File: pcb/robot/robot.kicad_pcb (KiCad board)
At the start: 4 copper layers, 80 x 70 mm, 314 parts, among them IC1 TPS22998RYZR, J1 USBC_Receptacle_SMD_RA, J2 Conn_01x05, J3 Conn_01x06_MountingPin, J4 USB4151-GF-C, J5 Conn_01x06_MountingPin, J8 Conn_01x02, J9 Conn_01x16, Q1 Q_NMOS_GDS, Q2 EFC8811R-TF, Q3 AS2312, Q4 YJL3416A, Q5 SN74AHC125RGYR, Q6 SN74AHC125RGYR, Q7 Q_NMOS_GDS, SW1 SW_SPST, U1 STWLC38JRM, U10 TPS63021DSJR, U11 XC6206PxxxMR, U12 BQ27742YZFR-G1, U13 MAX77976EFD+, U18 AP33771DKZ-13, U2 W25Q128JVS, U25 TVS0500DRV, U26 TPD1E05U06, U27 TPD1E05U06, U28 TPD1E05U06, U29 TPD1E05U06, U3 RP2040, U4 NCP3901, U5 LSF0102DCTR, U6 MAX77857BEWB+, U7 AP2502KTR-G1, U8 DRV8830DRCR, U9 DRV8830DRCR, Y1 ECS-120-8-36-CKM-TR3

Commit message: Fix reversed motor connector pins on J3/J5 (fixes #15)
Swap pins 1/6 (motor phase polarity) and 2/5 (encoder VCC/GND) on
both motor JST connectors (J3, J5), so standard JST cables work
without custom re-pinning and without needing a software-side
forward/backward negation workaround. Pins 3/4 (encoder A/B) left
untouched. PCB copper re-routed to match; verified 0 unconnected
items via DRC and no new ERC violations on J3/J5.

Firmware's negation workaround should be removed once this hardware
revision is in use, or the two corrections will cancel out.

Fix leftover note typo and grid nudge (follow-up to #3)

Correct CC jumper note in USB_PD_Module.kicad_sch to reference the
actual R3/R4 designators used, and nudge SW1 onto grid in
Protection.kicad_sch. No net changes.
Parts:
- moved R26 0.90 mm to (109.8, 148.6)
- moved R29 0.90 mm to (109.8, 150.1)
- moved NT16 0.10 mm to (111.3, 132.6)
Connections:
- J3 pad 1: /MOTORS/OUT_N2 -> /MOTORS/OUT_P2
- J3 pad 2: GND -> /MOTORS/ENC_VCC
- J3 pad 5: /MOTORS/ENC_VCC -> GND
- J3 pad 6: /MOTORS/OUT_P2 -> /MOTORS/OUT_N2
- J5 pad 1: /MOTORS/OUT_P1 -> /MOTORS/OUT_N1
- J5 pad 2: GND -> /MOTORS/ENC_VCC
- J5 pad 5: /MOTORS/ENC_VCC -> GND
- J5 pad 6: /MOTORS/OUT_N1 -> /MOTORS/OUT_P1
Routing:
- net /MOTORS/ENC_VCC: track 25.6 -> 31.7 mm
- net /MOTORS/VIO: track 33.4 -> 35.1 mm
- net Net-(NT16-Pad1): track 18.2 -> 19.7 mm
- net GND: vias 216 -> 214
- net /MOTORS/OUT_P2: vias 6 -> 5
- net /MOTORS/OUT_P1: vias 6 -> 5
- net /MOTORS/OUT_N1: vias 5 -> 6

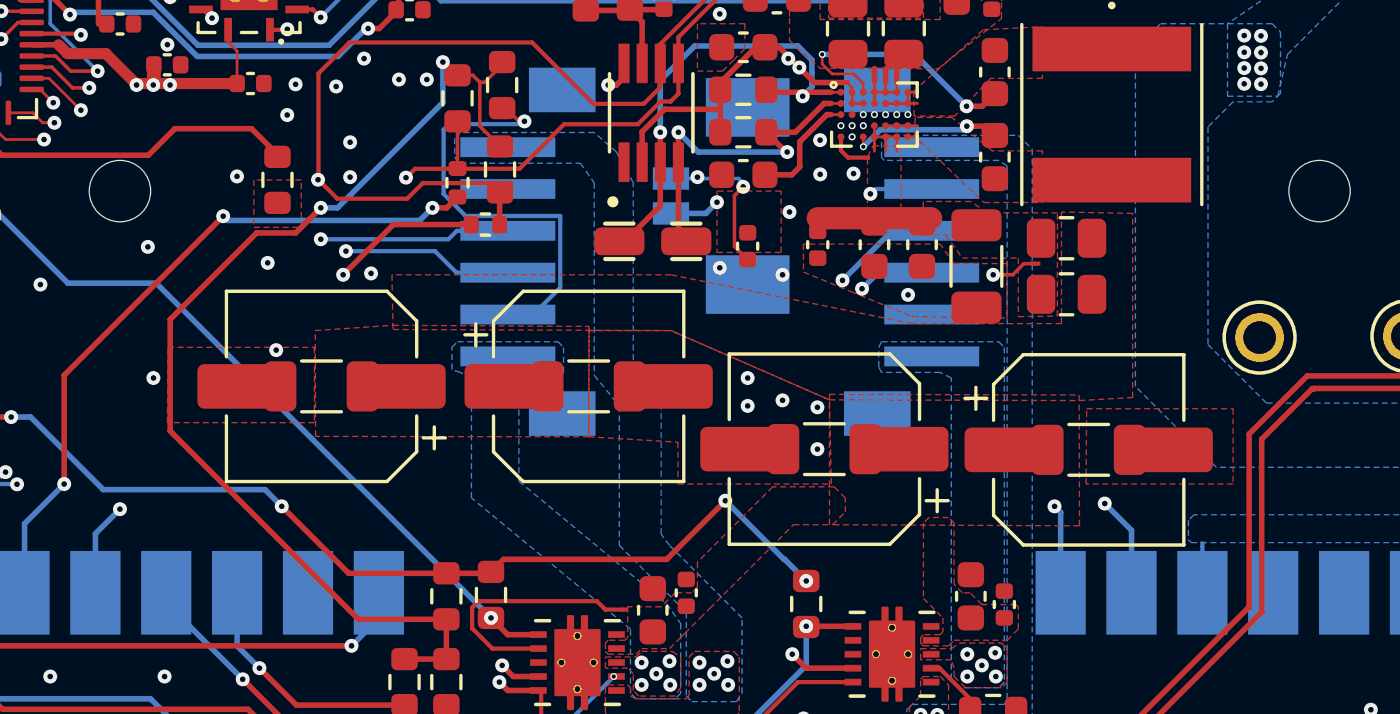
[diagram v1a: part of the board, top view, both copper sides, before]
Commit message: Remove unnecessary bulk caps C74/C86/C89/C90 (fixes #16)
Delete the 4 redundant 100uF bulk caps (VCC-GND, motor driver rail)
from both schematic and PCB to reclaim board space. Stress testing
(see #4 discussion) showed rail variation stays under 100mV even
without them, so the extra bulk capacitance added after the earlier
UVLO investigation is no longer needed.

Verified via ERC/DRC: same violation counts as before (314/7),
0 unconnected items - no regressions from the removal.
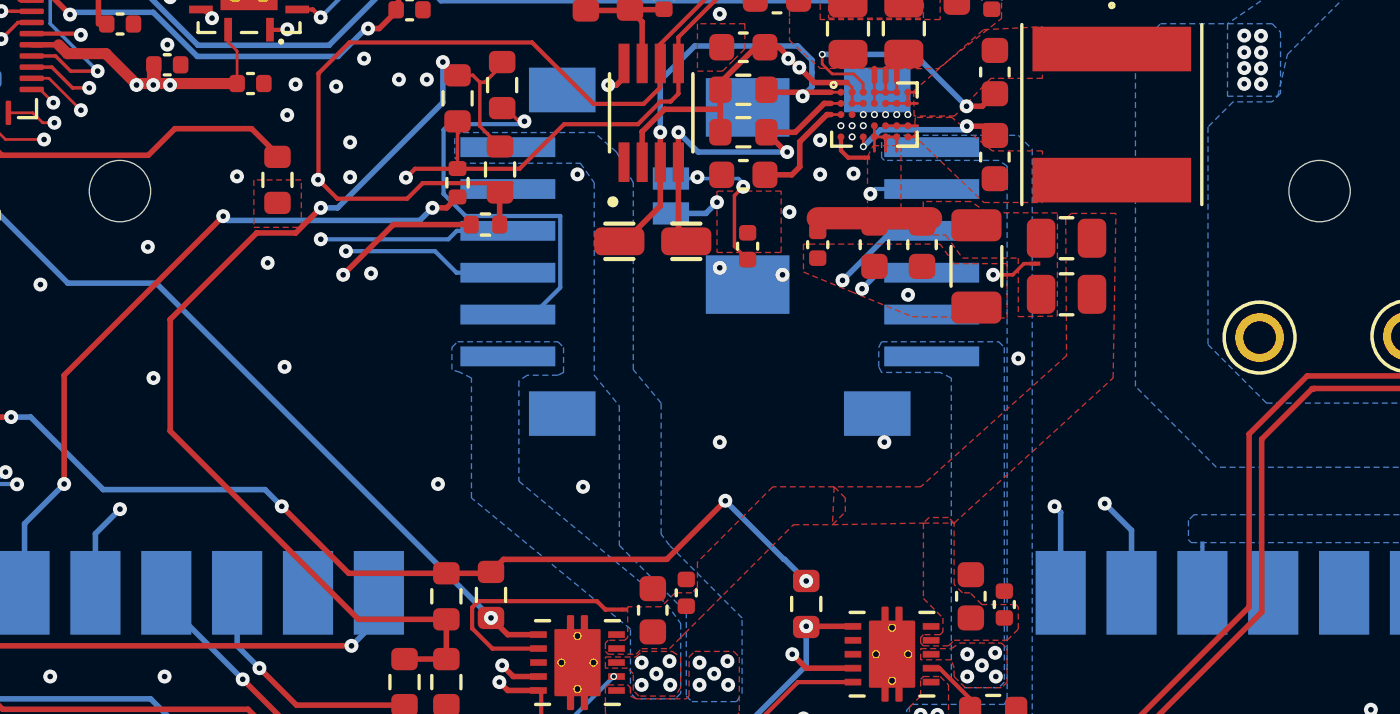
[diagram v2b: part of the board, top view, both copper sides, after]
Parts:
- removed C74, C86, C89, C90: 100uF, robot:CP_Elec_APXJ100ARA271MF61G
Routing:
- net GND: vias 214 -> 215
